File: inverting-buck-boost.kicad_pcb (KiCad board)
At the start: 2 copper layers, 15 x 18 mm, 12 parts, among them J1 Conn_01x03, U1 MT2499A

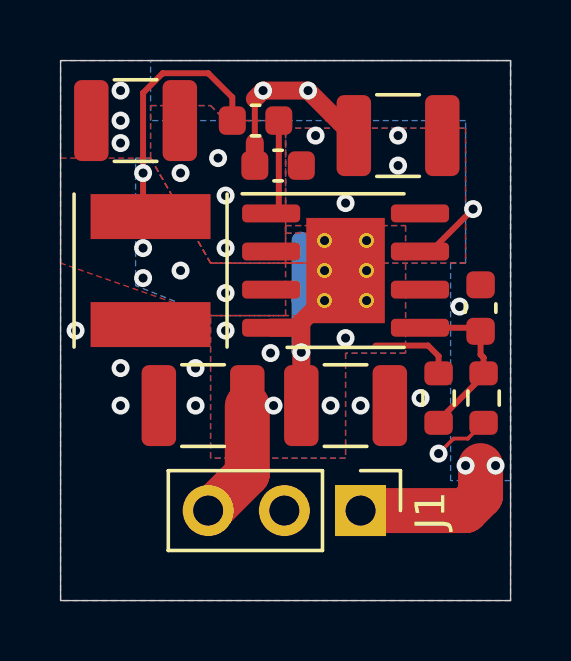
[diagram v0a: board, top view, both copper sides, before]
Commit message: Remove inductor fill
reduces parasitic capacitance
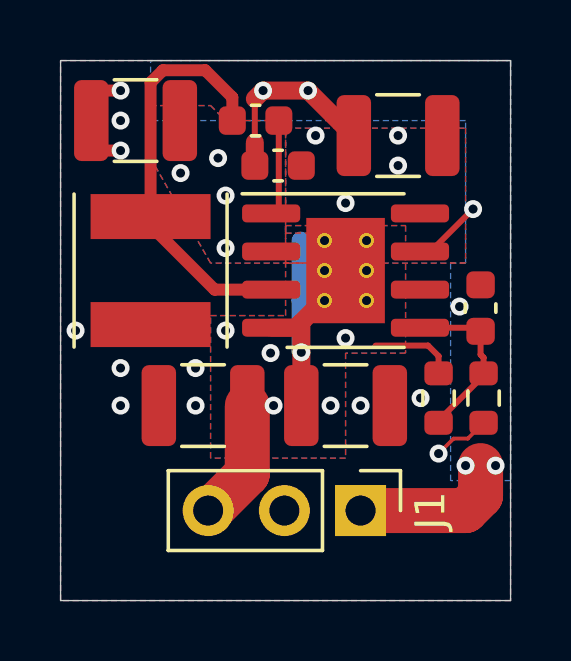
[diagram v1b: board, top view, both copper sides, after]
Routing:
- net /SW: track 8.23 -> 13.4 mm, vias 5 -> 0
- net GND: track 1.92 -> 2.92 mm
- removed copper zone on B.Cu, net /SW
- removed copper zone on F.Cu, net /SW
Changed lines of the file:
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@@
   )
   (gr_rect (start 111.5 73) (end 126.5 91) (layer "Edge.Cuts") (width 0.0381) (fill none))
+  (segment (start 113.5 74) (end 113 74) (width 0.4) (layer "F.Cu") (net 1))
+  (segment (start 113.5 76) (end 113 76) (width 0.4) (layer "F.Cu") (net 1))
   (segment (start 124.1 86.1) (end 124.598875 85.601125) (width 0.127) (layer "F.Cu") (net 1))
   (segment (start 125.6 85.075) (end 125.073875 85.601125) (width 0.127) (layer "F.Cu") (net 1))
@@
   (via (at 113.5 83.25) (size 0.6) (drill 0.3) (layers "F.Cu" "B.Cu") (free) (net 1))
   (via (at 116 83.25) (size 0.6) (drill 0.3) (layers "F.Cu" "B.Cu") (free) (net 1))
-  (via (at 113.5 74) (size 0.6) (drill 0.3) (layers "F.Cu" "B.Cu") (free) (net 1))
-  (via (at 113.5 75) (size 0.6) (drill 0.3) (layers "F.Cu" "B.Cu") (free) (net 1))
   (via (at 123.5 84.25) (size 0.6) (drill 0.3) (layers "F.Cu" "B.Cu") (free) (net 1))
   (via (at 121.5 84.5) (size 0.6) (drill 0.3) (layers "F.Cu" "B.Cu") (free) (net 1))
   (via (at 113.5 84.5) (size 0.6) (drill 0.3) (layers "F.Cu" "B.Cu") (free) (net 1))
-  (via (at 113.5 75.75) (size 0.6) (drill 0.3) (layers "F.Cu" "B.Cu") (free) (net 1))
   (via (at 116 84.5) (size 0.6) (drill 0.3) (layers "F.Cu" "B.Cu") (free) (net 1))
   (via (at 124.8 81.2) (size 0.6) (drill 0.3) (layers "F.Cu" "B.Cu") (free) (net 1))
+  (via (at 113.5 74) (size 0.6) (drill 0.3) (layers "F.Cu" "B.Cu") (free) (net 1))
+  (via (at 113.5 76) (size 0.6) (drill 0.3) (layers "F.Cu" "B.Cu") (free) (net 1))
   (via (at 112 82) (size 0.6) (drill 0.3) (layers "F.Cu" "B.Cu") (free) (net 1))
   (via (at 124.1 86.1) (size 0.6) (drill 0.3) (layers "F.Cu" "B.Cu") (free) (net 1))
+  (via (at 113.5 75) (size 0.6) (drill 0.3) (layers "F.Cu" "B.Cu") (free) (net 1))
   (segment (start 119.75 74) (end 121.25 75.5) (width 0.6) (layer "F.Cu") (net 2))
   (segment (start 125.25 77.95) (end 123.8 79.4) (width 0.2) (layer "F.Cu") (net 2))
@@
   (segment (start 119.5 82.7) (end 119.525 82.725) (width 0.6) (layer "B.Cu") (net 5))
   (segment (start 118.775 75) (end 118.775 77.975) (width 0.2) (layer "F.Cu") (net 6))
-  (segment (start 114.25 77.95) (end 114.25 76.75) (width 0.2) (layer "F.Cu") (net 7))
-  (segment (start 117.225 74.225) (end 117.225 75) (width 0.2) (layer "F.Cu") (net 7))
-  (segment (start 114.25 74.077) (end 114.904 73.423) (width 0.2) (layer "F.Cu") (net 7))
-  (segment (start 114.25 76.75) (end 114.25 74.077) (width 0.2) (layer "F.Cu") (net 7))
-  (segment (start 114.904 73.423) (end 116.423 73.423) (width 0.2) (layer "F.Cu") (net 7))
-  (segment (start 116.423 73.423) (end 117.225 74.225) (width 0.2) (layer "F.Cu") (net 7))
-  (via (at 117 80.75) (size 0.6) (drill 0.3) (layers "F.Cu" "B.Cu") (free) (net 7))
-  (via (at 115.5 80) (size 0.6) (drill 0.3) (layers "F.Cu" "B.Cu") (free) (net 7))
-  (via (at 114.25 80.25) (size 0.6) (drill 0.3) (layers "F.Cu" "B.Cu") (free) (net 7))
-  (via (at 114.25 79.25) (size 0.6) (drill 0.3) (layers "F.Cu" "B.Cu") (free) (net 7))
-  (via (at 114.25 76.75) (size 0.6) (drill 0.3) (layers "F.Cu" "B.Cu") (net 7))
+  (segment (start 117.225 74.225) (end 116.323 73.323) (width 0.4) (layer "F.Cu") (net 7))
+  (segment (start 114.5 78.2) (end 114.5 73.733999) (width 0.4) (layer "F.Cu") (net 7))
+  (segment (start 117.225 75) (end 117.225 74.225) (width 0.4) (layer "F.Cu") (net 7))
+  (segment (start 114.910999 73.323) (end 116.323 73.323) (width 0.4) (layer "F.Cu") (net 7))
+  (segment (start 114.5 73.733999) (end 114.910999 73.323) (width 0.4) (layer "F.Cu") (net 7))
+  (segment (start 118.52 80.635) (end 116.635 80.635) (width 0.4) (layer "F.Cu") (net 7))
+  (segment (start 116.635 80.635) (end 114.5 78.5) (width 0.4) (layer "F.Cu") (net 7))
   (segment (start 125.6 83.5) (end 124.1 85) (width 0.2) (layer "F.Cu") (net 8))
   (segment (start 123.48 81.905) (end 125.655 81.905) (width 0.2) (layer "F.Cu") (net 8))
@@
     )
   )
-  (zone (net 7) (net_name "/SW") (layer "F.Cu") (hatch edge 0.508)
-    (priority 2)
-    (connect_pads (clearance 0.2))
-    (min_thickness 0.2) (filled_areas_thickness no)
-    (fill yes (thermal_gap 0.2) (thermal_bridge_width 0.508))
+  (zone (net 0) (net_name "") (layer "F.Cu") (hatch edge 0.508)
+    (connect_pads (clearance 0))
+    (min_thickness 0.254)
+    (keepout (tracks allowed) (vias allowed) (pads allowed) (copperpour not_allowed) (footprints allowed))
+    (fill (thermal_gap 0.508) (thermal_bridge_width 0.508))
     (polygon
       (pts
-        (xy 116.5 79.75)
-        (xy 119.75 79.75)
-        (xy 119.75 81.5)
-        (xy 116.5 81.5)
-        (xy 111.5 79.75)
-        (xy 111.5 76.25)
-        (xy 114.5 76.25)
+        (xy 117 81.5)
+        (xy 111.5 81.5)
+        (xy 111.5 77)
+        (xy 114.5 77)
       )
     )
@@
       )
     )
-  )
-  (zone (net 7) (net_name "/SW") (layer "B.Cu") (hatch edge 0.508)
-    (priority 2)
-    (connect_pads (clearance 0.2))
-    (min_thickness 0.2) (filled_areas_thickness no)
-    (fill yes (thermal_gap 0.2) (thermal_bridge_width 0.508))
-    (polygon
-      (pts
-        (xy 116.5 79.75)
-        (xy 119.75 79.75)
-        (xy 119.75 81.5)
-        (xy 116.5 81.5)
-        (xy 114 80.5)
-        (xy 114 76.25)
-        (xy 114.5 76.25)
-      )
-    )
